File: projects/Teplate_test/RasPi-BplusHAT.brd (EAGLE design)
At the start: 65 x 56 mm, 1 part, among them K1 PIN20X2

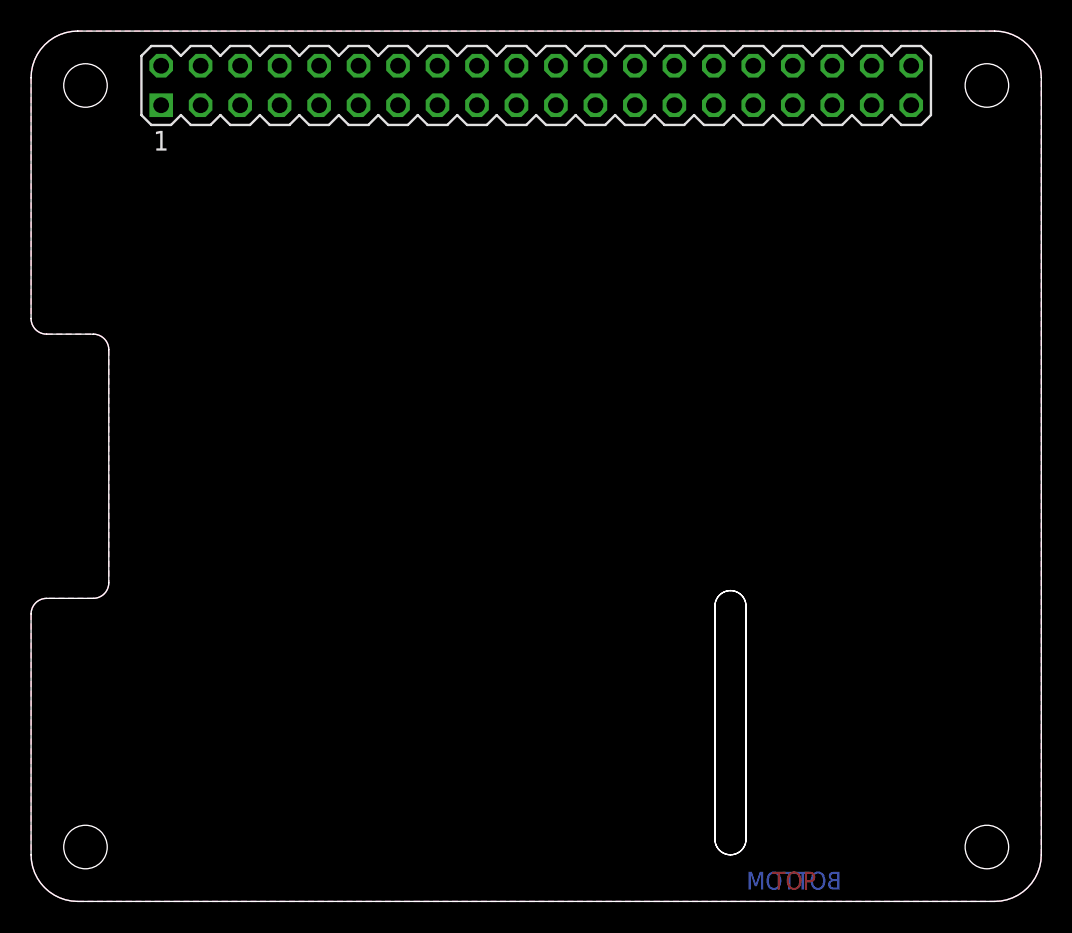
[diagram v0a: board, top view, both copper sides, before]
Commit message: Changed Template to be useful
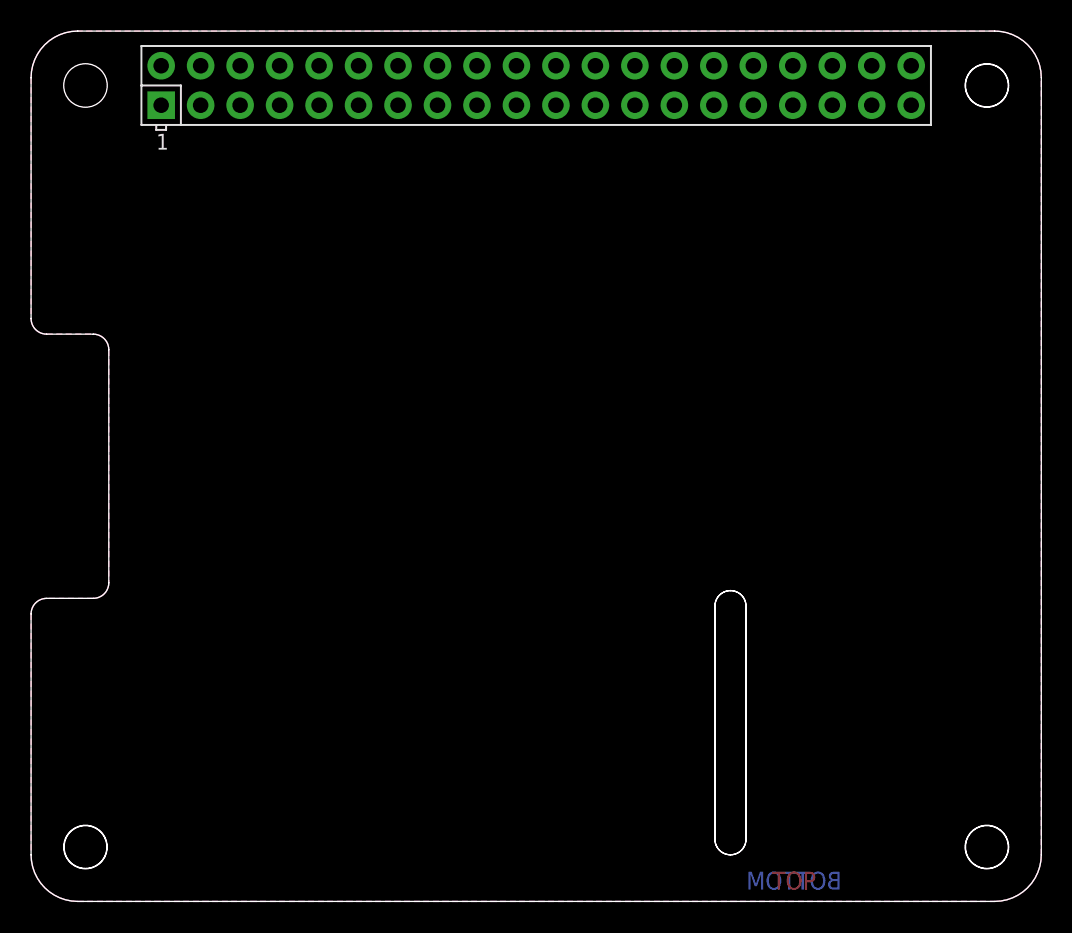
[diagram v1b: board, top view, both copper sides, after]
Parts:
- removed K1: PIN20X2, FLYFISH:PIN_20X2
- added X1: RASPI_BOARD_B+_E3, raspberrypi_bastelstube_v13:RASPI_BOARD_B+_EDGES_3DRILL
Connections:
- new net 3V3: X1.1
- new net 5V0: X1.2
- new net GND: X1.6
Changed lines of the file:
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@@
 <layer number="31" name="tCream" color="7" fill="4" visible="no" active="yes"/>
 <layer number="32" name="bCream" color="7" fill="5" visible="no" active="yes"/>
-<layer number="33" name="tFinish" color="6" fill="3" visible="no" active="yes"/>
+<layer number="33" name="tFinish" color="6" fill="3" visible="yes" active="yes"/>
 <layer number="34" name="bFinish" color="6" fill="6" visible="no" active="yes"/>
 <layer number="35" name="tGlue" color="7" fill="4" visible="no" active="yes"/>
@@
 </autorouter>
 <elements>
-<element name="K1" library="FLYFISH" package="PIN_20X2" value="PIN20X2" x="32.5" y="52.5" smashed="yes">
-<attribute name="VALUE" x="45.2" y="48.309" size="1.27" layer="27" ratio="10"/>
-</element>
+<element name="X1" library="raspberrypi_bastelstube_v13" package="RASPI_BOARD_B+_EDGES_3DRILL" value="RASPI_BOARD_B+_E3" x="0" y="0" smashed="yes"/>
 </elements>
 <signals>
@@
 <vertex x="0" y="18.5"/>
 </polygon>
+<contactref element="X1" pad="6"/>
+</signal>
+<signal name="5V0">
+<contactref element="X1" pad="2"/>
+</signal>
+<signal name="3V3">
+<contactref element="X1" pad="1"/>
 </signal>
 </signals>
